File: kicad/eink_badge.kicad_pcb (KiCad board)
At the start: 2 copper layers, 77.5 x 48.5 mm, 78 parts, among them CN2 B2B-PH-K-S, Q1 AO3400A, SW1 MST-12D18G2 SMD SLIDE SWITCH, U1 RP2350A, U10 TPS63060DSCR, U2 NCP1117-3.3_SOT223, U3 GT-USB-7010ASV, U4 W25Q128JVS, U5 YZA-009, U6 ABM8-272-T3_C20625731, U7 SM03B-SRSS-TB, U8 CY43-10UH, U9 BQ24040DSQR

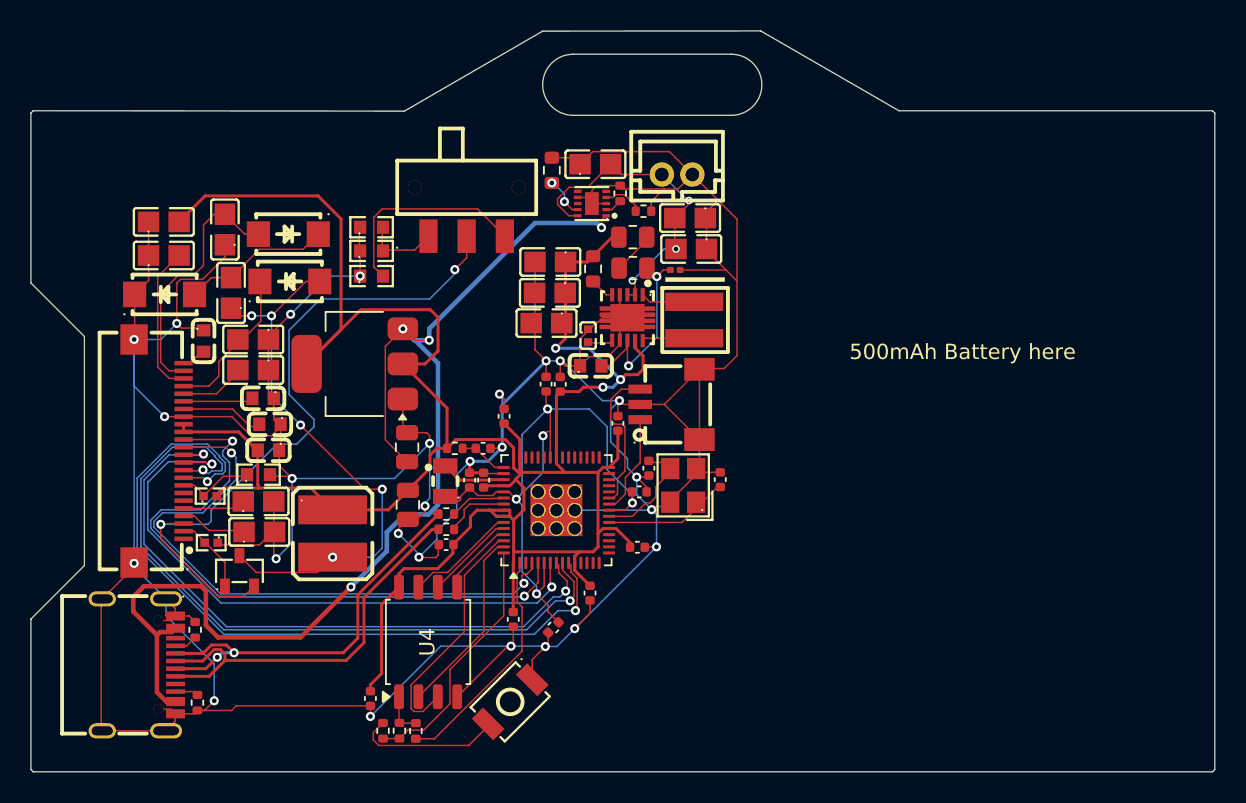
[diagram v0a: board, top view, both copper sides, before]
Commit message: Changed to use foorprint of 0603 0805 1005 metric for resistors and capacitors where possible
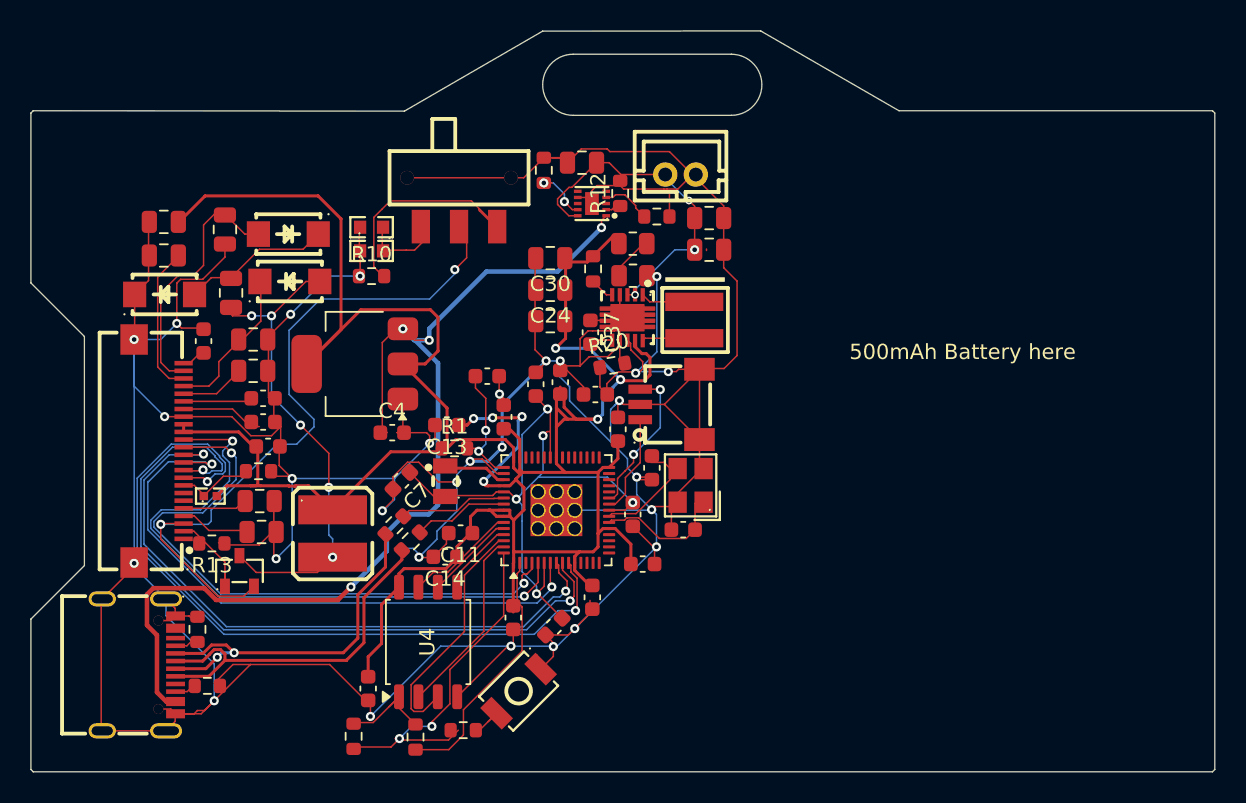
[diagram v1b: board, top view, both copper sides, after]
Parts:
- C1, C10, C11, C12, C13, C14, C15, C16, C17, C18, C2, C3, C6, C7, C8, C9: footprint Capacitor_SMD:C_0402_1005Metric -> Capacitor_SMD:C_0603_1608Metric
- C19, C20, C21, C22, C23, C25, C26, C27, C29: footprint easyeda2kicad:C0805 -> Capacitor_SMD:C_0805_2012Metric
- C24, C30, C35: value LMK212BJ226MG-T -> 22uF; footprint easyeda2kicad:C0805 -> Capacitor_SMD:C_0805_2012Metric
- C28, C36: value EMK212BJ106KG-T -> 10uF; footprint easyeda2kicad:C0805 -> Capacitor_SMD:C_0805_2012Metric
- C31, C32, C33, C34: value CL10A105KB8NNNC -> 1uF; footprint easyeda2kicad:C0603 -> Capacitor_SMD:C_0603_1608Metric
- C37: value CC0402KRX5R9BB104 -> 0.1uF; footprint easyeda2kicad:C0402 -> Capacitor_SMD:C_0603_1608Metric
- C38: value CL10C100JB8NNNC -> 10pF; footprint easyeda2kicad:C0603 -> Capacitor_SMD:C_0603_1608Metric
- C4, C5: footprint Capacitor_SMD:C_0805_2012Metric -> Capacitor_SMD:C_0603_1608Metric
- R1, R12, R2, R3, R4, R5, R6, R7, R8, R9: footprint Resistor_SMD:R_0402_1005Metric -> Resistor_SMD:R_0603_1608Metric
- R10, R11: value 0603WAF220KT5E -> 2.2; footprint easyeda2kicad:R0603 -> Resistor_SMD:R_0603_1608Metric
- R13: value 0402WGF1002TCE -> 10k; footprint easyeda2kicad:R0402 -> Resistor_SMD:R_0603_1608Metric
- R14: value 0402WGF1002TCE -> 10k
- R15, R16: value 0603WAF100KT5E -> 1
- R20: footprint Resistor_SMD:R_0201_0603Metric -> Resistor_SMD:R_0603_1608Metric
- moved C10 15.8 mm to (116.7, 67.0), turned to 90 degrees
- moved C7 15.6 mm to (106.3, 73.4), turned to -135 degrees
- moved C1 11.8 mm to (122.0, 78.9), turned to 0 degrees
- moved C11 11.7 mm to (110.1, 76.9), turned to 180 degrees
- moved C13 11.2 mm to (109.2, 69.8), turned to 180 degrees
- moved C2 10.9 mm to (121.4, 75.7), turned to -90 degrees
- moved C9 10.2 mm to (118.8, 81.1), turned to -90 degrees
- moved C14 9.98 mm to (109.1, 78.4), turned to 180 degrees
- moved C5 8.51 mm to (113.0, 69.3), turned to 90 degrees
- moved C15 7.83 mm to (120.4, 70.1), turned to 90 degrees
- moved R20 7.48 mm to (120.1, 65.9), turned to 10 degrees
- moved C12 5.28 mm to (113.6, 82.4)
- moved R9 5.25 mm to (110.3, 89.8), turned to 180 degrees
- moved C3 4.73 mm to (111.9, 66.6)
- moved C18 4.08 mm to (124.7, 76.7), turned to 0 degrees
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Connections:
- net /BS renamed /E Ink/BS
- net /Batt+ renamed /Battery Charger/Batt+
- net /D+ renamed /Root/D+
- net /D- renamed /Root/D-
- net /GDR renamed /E Ink/GDR
- net /GPIO0 renamed /Root/GPIO0
- net /PREVGH renamed /E Ink/PREVGH
- net /PREVGL renamed /E Ink/PREVGL
- net /QSPI_SCLK renamed /Root/QSPI_SCLK
- net /QSPI_SD0 renamed /Root/QSPI_SD0
- net /QSPI_SD1 renamed /Root/QSPI_SD1
- net /QSPI_SD2 renamed /Root/QSPI_SD2
- net /QSPI_SD3 renamed /Root/QSPI_SD3
- net /QSPI_SS renamed /Root/QSPI_SS
- net /RESE renamed /E Ink/RESE
- net /SWCLK renamed /Root/SWCLK
- net /SWDIO renamed /Root/SWDIO
- net /VCOM renamed /E Ink/VCOM
- net /VREG_AVDD renamed /Root/VREG_AVDD
- net /VREG_LX renamed /Root/VREG_LX
- net /XIN renamed /Root/XIN
- net /XOUT renamed /Root/XOUT
- C4 pad 1: VBUS -> Net-(U2-VI)
- FPC1 pad 10: /RES -> /E Ink/RES
- FPC1 pad 11: /D/C -> /E Ink/D/C
- FPC1 pad 12: /CS -> /E Ink/CS
- FPC1 pad 13: /SCLK -> /E Ink/SCLK
- FPC1 pad 14: /SDI -> /E Ink/SDI
- FPC1 pad 9: /BUSY -> /E Ink/BUSY
- U1 pad 10: /BUSY -> /Root/BUSY
- U1 pad 4: /SCLK -> /Root/SCLK
- U1 pad 5: /SDI -> /Root/SDI
- U1 pad 7: /D/C -> /Root/D/C
- U1 pad 8: /CS -> /Root/CS
- U1 pad 9: /RES -> /Root/RES
- U2 pad 3: VBUS -> Net-(U2-VI)
- U3 pad : GND -> (no net)
- U3 pad A4B9: VBUS -> Net-(U3-VBUS-PadA4B9)
- U3 pad B4A9: VBUS -> Net-(U3-VBUS-PadB4A9)
- U9 pad 1: VBUS -> Net-(U9-IN)
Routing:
- net (no net): track 0.00 -> 283.5 mm, vias 0 -> 14
- net VBUS: track 78.5 -> 0.00 mm, vias 4 -> 0
- net /BUSY: track 50.7 -> 0.00 mm, vias 2 -> 0
- net /RES: track 48.4 -> 0.00 mm, vias 2 -> 0
- net /CS: track 43.1 -> 0.00 mm, vias 2 -> 0
- net /SDI: track 41.9 -> 0.00 mm, vias 2 -> 0
- net /D/C: track 40.4 -> 0.00 mm, vias 2 -> 0
- net /SCLK: track 40.1 -> 0.00 mm, vias 2 -> 0
- net GND: track 346.3 -> 378.9 mm, vias 26 -> 27
- net Net-(U2-VI): track 0.00 -> 28.4 mm, vias 0 -> 1
- net Net-(U3-VBUS-PadB4A9): track 0.00 -> 22.3 mm, vias 0 -> 1
- net +3V3: track 167.0 -> 185.0 mm, vias 3 -> 7
- net /Root/QSPI_SS: track 16.7 -> 23.4 mm, vias 0 -> 2
- net Net-(R9-Pad1): track 9.15 -> 2.60 mm
- net /Root/VREG_AVDD: track 3.21 -> 8.59 mm, vias 0 -> 2
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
